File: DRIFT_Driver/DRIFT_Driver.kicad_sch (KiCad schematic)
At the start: 6 parts, among them IC2 AMS1117-3.3, IC4 ESP32-S3-WROOM-1-N4

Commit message: Finished majority of component implementations
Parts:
- removed C21: 0.1uF, symbol Device:C
- removed IC2: AMS1117-3.3, SOT229P700X180-4N, symbol AMS1117-3_3:AMS1117-3.3
- added C18, C26, C27, C29: 10u, Capacitor_SMD:C_0402_1005Metric, symbol Device:C_Small
- added C20, C21, C22, C23, C28, C32: 0.1u, Capacitor_SMD:C_0402_1005Metric, symbol Device:C_Small
- added C24, C25: 20p, Capacitor_SMD:C_0402_1005Metric, symbol Device:C_Small
- added D3: BAT60A, Diode_SMD:D_SOD-323, symbol Diode:BAT60A
- added D4: LED, LED_SMD:LED_0603_1608Metric, symbol Device:LED
- added J1: USB4105-GF-A, Touchstone:GCT_USB4105-GF-A, symbol USB4105-GF-A:USB4105-GF-A
- added R30: 500, Resistor_SMD:R_0402_1005Metric, symbol Device:R
- added R31, R32: 5.1kΩ, Resistor_SMD:R_0603_1608Metric_Pad0.98x0.95mm_HandSolder, symbol Device:R
- added R33, R34: 22Ω, Resistor_SMD:R_0603_1608Metric, symbol Device:R_Small
- added SW1, SW2: SW_SPST, Button_Switch_THT:SW_PUSH_6mm, symbol Switch:SW_SPST
- added U8: USBLC6-2SC6, Package_TO_SOT_SMD:SOT-23-6, symbol Power_Protection:USBLC6-2SC6
- added U9: MIC5365-3.3YC5, Package_TO_SOT_SMD:SOT-353_SC-70-5, symbol Regulator_Linear:MIC5365-3.3YC5
- IC4: footprint ESP32S3WROOM1N4 -> Touchstone:ESP32S3WROOM1N4
- R27, R28, R29: footprint (none) -> Resistor_SMD:R_0402_1005Metric
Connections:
- net +3.3V: now also C21.2, C23.1, C26.2, C29.1, D4.2 (A), U9.5 (VOUT)
- net CHIP_PU: now also R29.2, C28.1, C32.1, SW2.2 (B)
- net GND: now also C18.1, C20.2, C21.1, C22.2, C23.2, C24.2, C25.2, C26.1, C27.2, C28.2, C29.2, C32.2, J1.A1_B12 (GND), J1.B1_A12 (GND__1), J1.SH1 (SHELL_GND), J1.SH2 (SHELL_GND__1), J1.SH3 (SHELL_GND__2), J1.SH4 (SHELL_GND__3), R30.2, R31.2, R32.2, SW1.1 (A), SW2.1 (A), U8.2 (GND), U9.2 (GND)
- net at IC4.12 (IO8): no longer R29.2
- net at IC4.38 (IO2): no longer R28.2
- net D-: now reaches IC4.13 (IO19)
- net D-: now also R34.1
- net D+: now reaches IC4.14 (IO20)
- net D+: now also R33.1
- net GPIO0: now reaches IC4.27 (IO0)
- net GPIO0: now also R28.2, C20.1, SW1.2 (B)
- net IO9: no longer names the net of IC4.17 (IO9)
- new net: D4.1 (K), R30.1
- new net: C18.2, D3.2 (A), J1.A4_B9 (VBUS), J1.B4_A9 (VBUS__1), U8.5 (VBUS)
- new net: J1.A5 (CC1), R31.1
- new net: J1.A6 (DP1), J1.B6 (DP2), U8.1 (I/O1)
- new net: J1.A7 (DN1), J1.B7 (DN2), U8.3 (I/O2)
- new net: J1.B5 (CC2), R32.1
- new net: C25.1, R34.2, U8.4 (I/O2)
- new net: C24.1, R33.2, U8.6 (I/O1)
- new net +5V: C22.1, C27.1, D3.1 (K), U9.1 (VIN), U9.3 (EN)
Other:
- sheet Driver_Unit1: file Driver_Unit.kicBd_sch -> Driver_Unit.kicad_sch
- moved on the sheet: IC4, R27, R28

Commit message: Finished schematic first draft
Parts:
- added J2, J5: Conn_01x04, Connector_PinHeader_2.54mm:PinHeader_1x04_P2.54mm_Vertical, symbol Connector_Generic:Conn_01x04
- added J3: Conn_01x06, Connector_PinSocket_2.54mm:PinSocket_1x06_P2.54mm_Horizontal, symbol Connector_Generic:Conn_01x06
- added J4: Conn_01x06, Connector_PinHeader_2.54mm:PinHeader_1x06_P2.54mm_Horizontal, symbol Connector_Generic:Conn_01x06
- added J6: Conn_01x02, TerminalBlock:TerminalBlock_Altech_AK300-2_P5.00mm, symbol Connector_Generic:Conn_01x02
- added J7, J8: Conn_01x03, Connector_PinHeader_2.54mm:PinHeader_1x03_P2.54mm_Vertical, symbol Connector_Generic:Conn_01x03
- added R35, R36: 10k, Resistor_SMD:R_0402_1005Metric, symbol Device:R
- R31: footprint Resistor_SMD:R_0603_1608Metric_Pad0.98x0.95mm_HandSolder -> Resistor_SMD:R_0402_1005Metric_Pad0.72x0.64mm_HandSolder
- R32: footprint Resistor_SMD:R_0603_1608Metric_Pad0.98x0.95mm_HandSolder -> Resistor_SMD:R_0402_1005Metric
- R33, R34: footprint Resistor_SMD:R_0603_1608Metric -> Resistor_SMD:R_0402_1005Metric
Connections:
- net +3.3V: now also J2.1 (Pin_1), J5.1 (Pin_1), R35.2, R36.2
- net +5V: now also J3.1 (Pin_1), J4.1 (Pin_1)
- net GND: now also J2.2 (Pin_2), J3.2 (Pin_2), J4.2 (Pin_2), J5.2 (Pin_2), J6.2 (Pin_2)
- net OUT1A: now also J7.1 (Pin_1)
- net OUT1B: now also J8.1 (Pin_1)
- net OUT2A: now also J7.2 (Pin_2)
- net OUT2B: now also J8.2 (Pin_2)
- net OUT3A: now also J7.3 (Pin_3)
- net OUT3B: now also J8.3 (Pin_3)
- net SENSE1A: now also IC4.29 (IO36)
- net SENSE1B: now also IC4.4 (IO4)
- net SENSE2A: now also IC4.30 (IO37)
- net SENSE2B: now also IC4.38 (IO2)
- net SDA2: now reaches IC4.10 (IO17)
- net SDA2: now also J5.3 (Pin_3)
- net SCL2: now reaches IC4.11 (IO18)
- net SCL2: now also J5.4 (Pin_4)
- net MISO: now reaches IC4.20 (IO12)
- net MISO: now also J4.3 (Pin_3)
- net MOSI: now reaches IC4.21 (IO13)
- net MOSI: now also J3.3 (Pin_3)
- net CLK: now reaches IC4.22 (IO14)
- net CLK: now also J3.5 (Pin_5), J4.5 (Pin_5)
- net SDA1: now reaches IC4.5 (IO5)
- net SDA1: now also J2.3 (Pin_3)
- net SCL1: now reaches IC4.6 (IO6)
- net SCL1: now also J2.4 (Pin_4)
- net CS: now reaches IC4.8 (IO15)
- net CS: now also J3.6 (Pin_6), J4.6 (Pin_6), R35.1, R36.1
- new net LOOP: J3.4 (Pin_4), J4.4 (Pin_4)
- new net VMOT: J6.1 (Pin_1)
- no-connect marks 0 -> 1

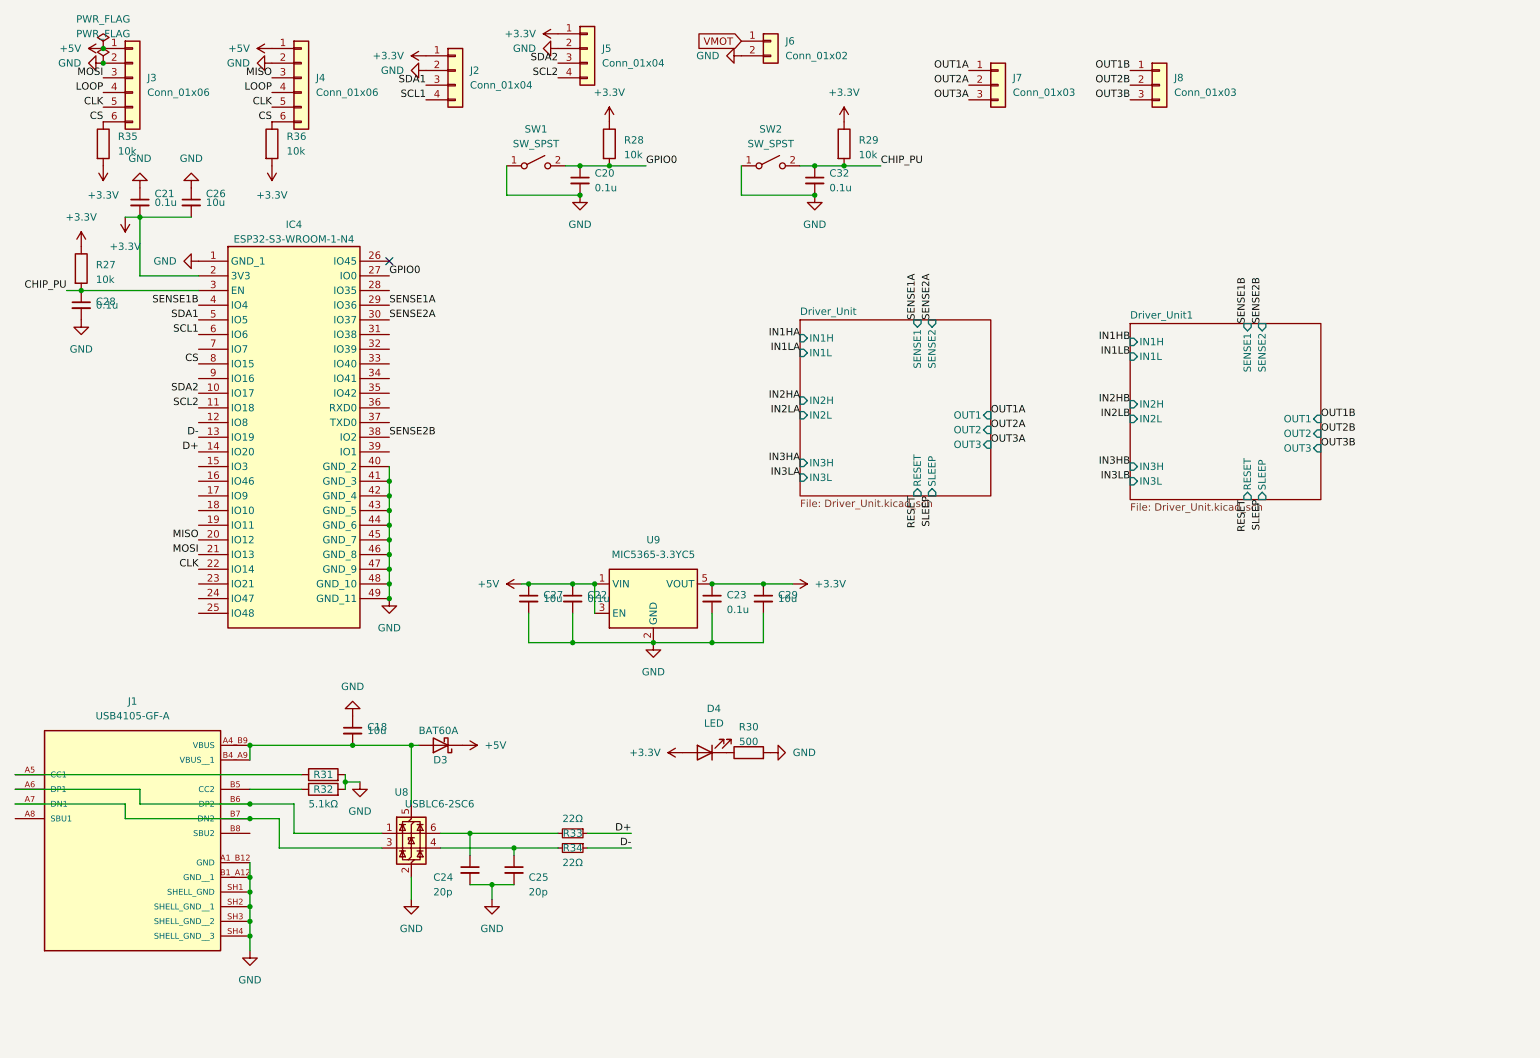
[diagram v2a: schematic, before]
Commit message: Changed annotations and fixed capacitor ratings
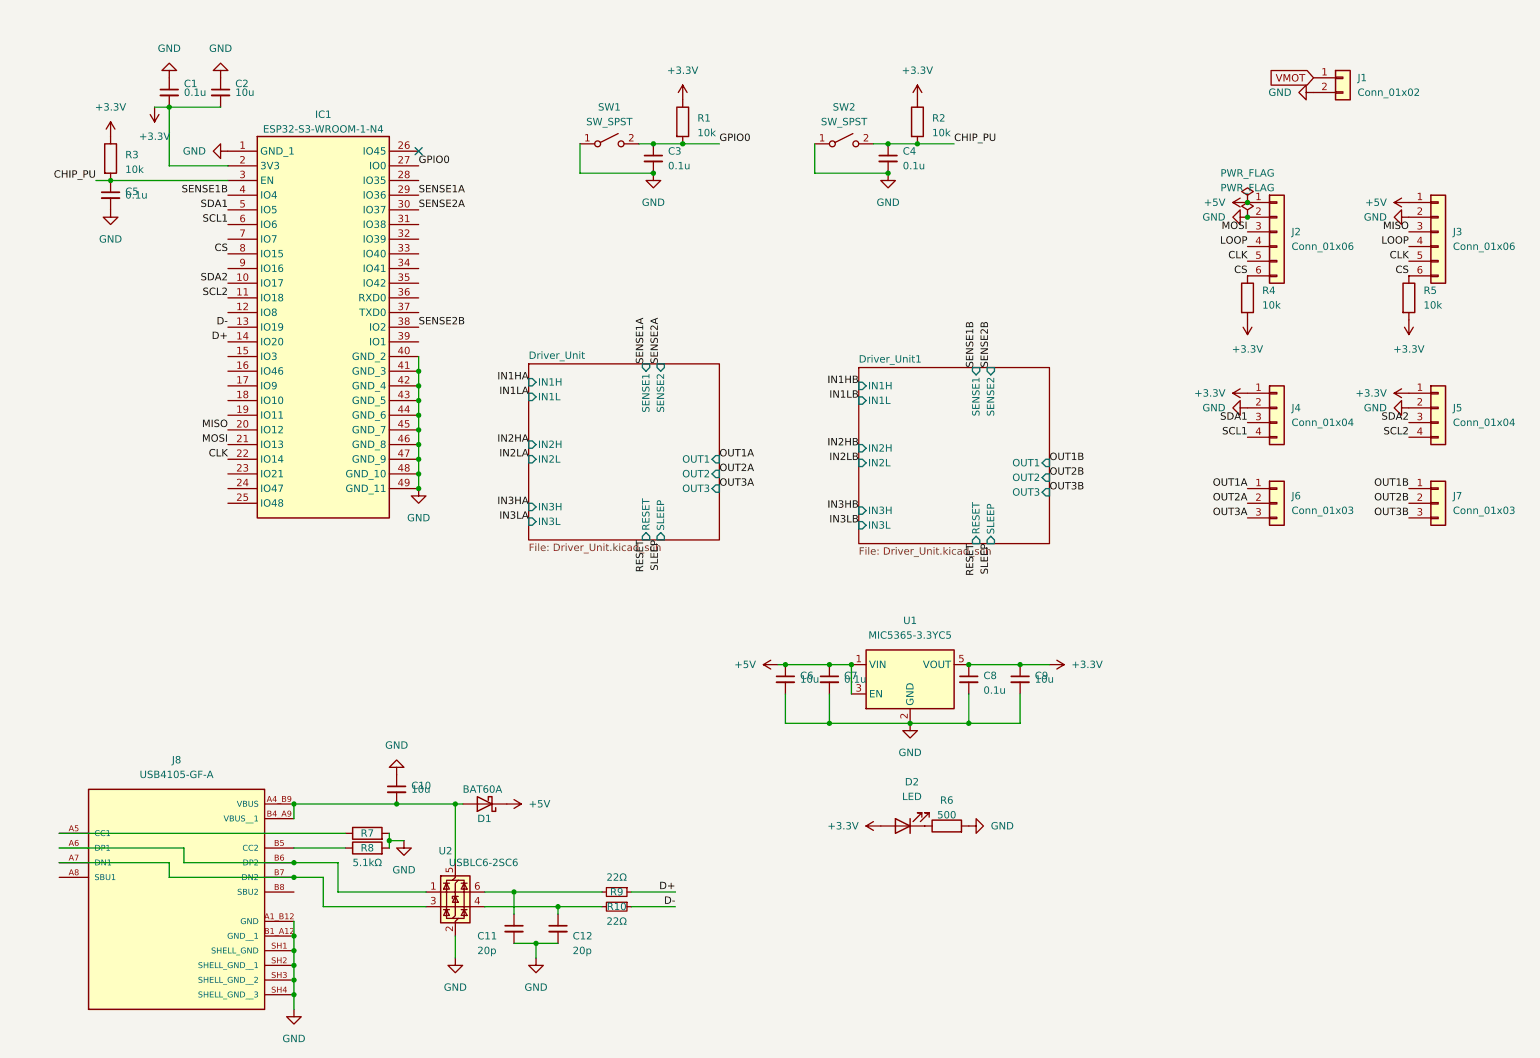
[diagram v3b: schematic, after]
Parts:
- C10: renamed from C18; footprint Capacitor_SMD:C_0402_1005Metric -> Capacitor_SMD:C_0805_2012Metric
- C2: renamed from C26; footprint Capacitor_SMD:C_0402_1005Metric -> Capacitor_SMD:C_0805_2012Metric
- C6: renamed from C27; footprint Capacitor_SMD:C_0402_1005Metric -> Capacitor_SMD:C_0805_2012Metric
- C9: renamed from C29; footprint Capacitor_SMD:C_0402_1005Metric -> Capacitor_SMD:C_0805_2012Metric
- J1: renamed from J6; footprint TerminalBlock:TerminalBlock_Altech_AK300-2_P5.00mm -> TerminalBlock:TerminalBlock_MaiXu_MX126-5.0-02P_1x02_P5.00mm
- renumbered C21 to C1, C24 to C11, C25 to C12, C20 to C3, C32 to C4, C28 to C5, C22 to C7, C23 to C8, D3 to D1, D4 to D2, IC4 to IC1, J3 to J2, J4 to J3, J2 to J4, J7 to J6, J8 to J7, J1 to J8, R28 to R1, R34 to R10, R29 to R2, R27 to R3, R35 to R4, R36 to R5, R30 to R6, R31 to R7, R32 to R8, R33 to R9, U9 to U1, U8 to U2
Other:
- moved on the sheet: C1, C10, C11, C12, C2, C3, C4, C5, C6, C7, C8, C9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

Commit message: Added second terminal block
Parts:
- added J2: Conn_01x02, TerminalBlock:TerminalBlock_MaiXu_MX126-5.0-02P_1x02_P5.00mm, symbol Connector_Generic:Conn_01x02
- renumbered J2 to J3, J3 to J4, J4 to J5, J5 to J6, J6 to J7, J7 to J8, J8 to J9
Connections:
- net GND: now also J2.2 (Pin_2)
- net VMOT: now also J2.1 (Pin_1)
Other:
- moved on the sheet: J1

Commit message: Some progress on motor driver unit layout
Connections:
- net IN1HA: now also IC1.7 (IO7)
- net IN1HB: now also IC1.18 (IO10)
- net IN1LA: now also IC1.9 (IO16)
- net IN1LB: now also IC1.19 (IO11)
- net IN2HA: now also IC1.12 (IO8)
- net IN2HB: now also IC1.23 (IO21)
- net IN2LA: now also IC1.15 (IO3)
- net IN2LB: now also IC1.24 (IO47)
- net IN3HA: now also IC1.16 (IO46)
- net IN3HB: now also IC1.25 (IO48)
- net IN3LA: now also IC1.17 (IO9)
- net IN3LB: now also IC1.26 (IO45)
- no-connect marks 1 -> 0
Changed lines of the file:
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@@
 		(color 0 0 0 0)
-	)
-	(no_connect
-		(at 81.28 34.29)
 	)
 	(wire
@@
 		)
 	)
+	(label "IN3HA"
+		(at 48.26 72.39 180)
+		(effects
+			(font
+				(size 1.27 1.27)
+			)
+			(justify right bottom)
+		)
+	)
 	(label "IN1HA"
 		(at 100.33 74.295 180)
@@
 		)
 	)
+	(label "IN2HA"
+		(at 48.26 62.23 180)
+		(effects
+			(font
+				(size 1.27 1.27)
+			)
+			(justify right bottom)
+		)
+	)
 	(label "GPIO0"
 		(at 133.35 33.02 0)
@@
 		)
 	)
+	(label "IN2LB"
+		(at 48.26 92.71 180)
+		(effects
+			(font
+				(size 1.27 1.27)
+			)
+			(justify right bottom)
+		)
+	)
 	(label "IN3HA"
 		(at 100.33 95.885 180)
@@
 		)
 	)
+	(label "IN2HB"
+		(at 48.26 90.17 180)
+		(effects
+			(font
+				(size 1.27 1.27)
+			)
+			(justify right bottom)
+		)
+	)
+	(label "IN1LB"
+		(at 48.26 80.01 180)
+		(effects
+			(font
+				(size 1.27 1.27)
+			)
+			(justify right bottom)
+		)
+	)
 	(label "SENSE2A"
 		(at 81.28 44.45 0)
@@
 		)
 	)
+	(label "IN1HB"
+		(at 48.26 77.47 180)
+		(effects
+			(font
+				(size 1.27 1.27)
+			)
+			(justify right bottom)
+		)
+	)
 	(label "SDA1"
 		(at 224.79 81.28 180)
@@
 		)
 	)
+	(label "IN3LA"
+		(at 48.26 74.93 180)
+		(effects
+			(font
+				(size 1.27 1.27)
+			)
+			(justify right bottom)
+		)
+	)
 	(label "SCL2"
 		(at 48.26 59.69 180)
@@
 		)
 	)
+	(label "IN2LA"
+		(at 48.26 69.85 180)
+		(effects
+			(font
+				(size 1.27 1.27)
+			)
+			(justify right bottom)
+		)
+	)
 	(label "OUT2B"
 		(at 252.73 95.25 180)
@@
 		)
 	)
+	(label "IN1HA"
+		(at 48.26 49.53 180)
+		(effects
+			(font
+				(size 1.27 1.27)
+			)
+			(justify right bottom)
+		)
+	)
 	(label "OUT3A"
 		(at 133.35 92.71 0)
@@
 		)
 	)
+	(label "IN3LB"
+		(at 81.28 34.29 0)
+		(effects
+			(font
+				(size 1.27 1.27)
+			)
+			(justify left bottom)
+		)
+	)
 	(label "SLEEP"
 		(at 180.34 102.235 270)
@@
 		)
 	)
+	(label "IN1LA"
+		(at 48.26 54.61 180)
+		(effects
+			(font
+				(size 1.27 1.27)
+			)
+			(justify right bottom)
+		)
+	)
 	(label "SENSE1B"
 		(at 177.8 71.755 90)
@@
 		(effects
 			(font
+				(size 1.27 1.27)
+			)
+			(justify right bottom)
+		)
+	)
+	(label "IN3HB"
+		(at 48.26 95.25 180)
+		(effects
+			(font
